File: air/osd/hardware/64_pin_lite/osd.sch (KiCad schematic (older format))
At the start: 0 parts

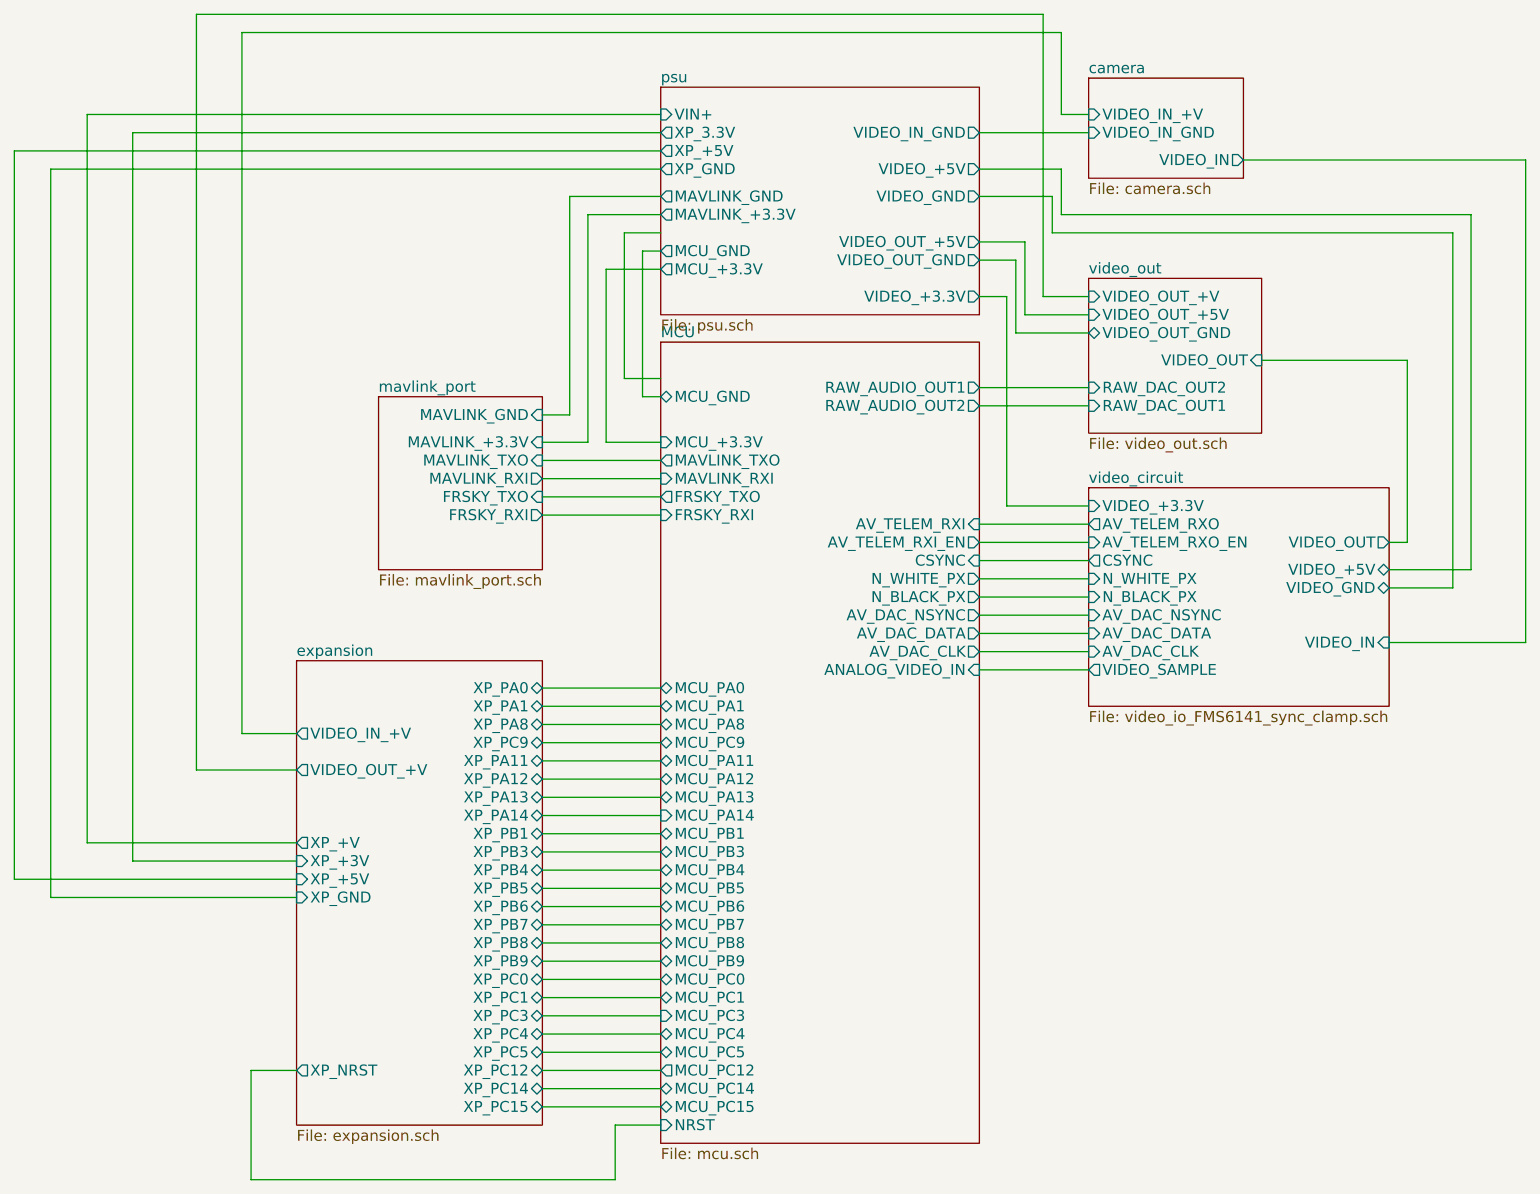
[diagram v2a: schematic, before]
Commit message: added links for isolted port and other mods
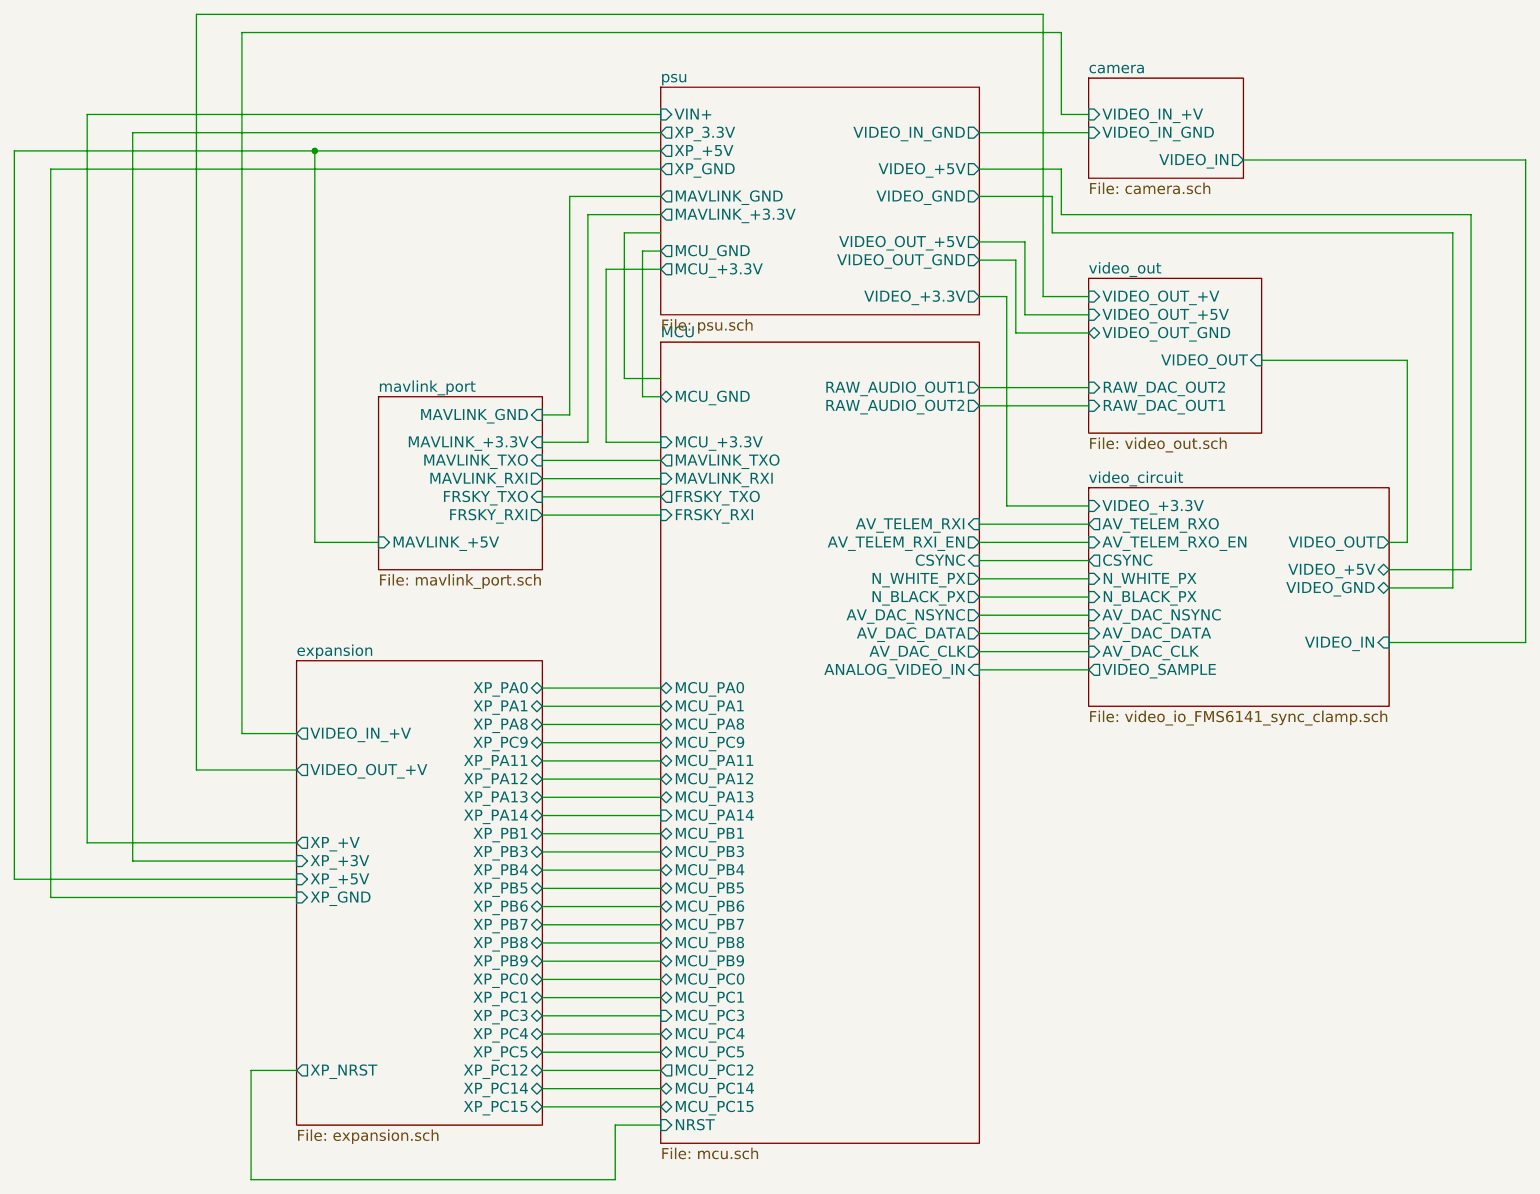
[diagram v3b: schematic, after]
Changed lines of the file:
@@
-EESchema Schematic File Version 2  date Sun 30 Nov 2014 15:34:12 GMT
+EESchema Schematic File Version 2  date Mon 01 Dec 2014 08:28:41 GMT
 LIBS:power
 LIBS:device
@@
 Sheet 1 8
 Title ""
-Date "30 nov 2014"
+Date "1 dec 2014"
 Rev ""
 Comp ""
@@
 Comment4 ""
 $EndDescr
-Wire Wire Line
-	4700 6800 4450 6800
-Wire Wire Line
-	4450 6800 4450 7100
-Wire Wire Line
-	4450 7100 2450 7100
-Wire Wire Line
-	2450 7100 2450 6500
-Wire Wire Line
-	2450 6500 2700 6500
-Wire Wire Line
-	4700 1350 1800 1350
-Wire Wire Line
-	1800 1350 1800 5350
-Wire Wire Line
-	1800 5350 2700 5350
-Wire Wire Line
-	4700 2100 4400 2100
-Wire Wire Line
-	4400 2100 4400 3050
-Wire Wire Line
-	4400 3050 4700 3050
-Wire Wire Line
-	7050 1250 6900 1250
-Wire Wire Line
-	6900 1250 6900 800
-Wire Wire Line
-	6900 800  2400 800
-Wire Wire Line
-	2400 800  2400 4650
-Wire Wire Line
-	2400 4650 2700 4650
-Wire Wire Line
-	4700 1250 1550 1250
-Wire Wire Line
-	1550 1250 1550 5250
-Wire Wire Line
-	1550 5250 2700 5250
+Connection ~ 2800 1450
+Wire Wire Line
+	2800 1450 2800 3600
+Wire Wire Line
+	2800 3600 3150 3600
+Wire Wire Line
+	4700 2700 4500 2700
+Wire Wire Line
+	7050 3400 6600 3400
+Wire Wire Line
+	6600 3400 6600 2250
+Wire Wire Line
+	6600 2250 6450 2250
+Wire Wire Line
+	4700 1800 4300 1800
+Wire Wire Line
+	4300 1800 4300 3050
+Wire Wire Line
+	4300 3050 4050 3050
+Wire Wire Line
+	7050 2250 6800 2250
+Wire Wire Line
+	6800 2250 6800 700
+Wire Wire Line
+	6800 700  2150 700
+Wire Wire Line
+	2150 700  2150 4850
+Wire Wire Line
+	2150 4850 2700 4850
+Wire Wire Line
+	4050 2900 4200 2900
+Wire Wire Line
+	4200 2900 4200 1700
+Wire Wire Line
+	4200 1700 4700 1700
+Wire Wire Line
+	7050 2750 6450 2750
+Wire Wire Line
+	4700 1550 1350 1550
+Wire Wire Line
+	1350 1550 1350 5550
+Wire Wire Line
+	1350 5550 2700 5550
+Wire Wire Line
+	4700 3450 4050 3450
+Wire Wire Line
+	4700 3250 4050 3250
+Wire Wire Line
+	4700 1900 4500 1900
+Wire Wire Line
+	4500 1900 4500 2700
+Wire Wire Line
+	4050 6600 4700 6600
+Wire Wire Line
+	4050 6400 4700 6400
+Wire Wire Line
+	4050 6200 4700 6200
+Wire Wire Line
+	4050 6000 4700 6000
+Wire Wire Line
+	4050 5800 4700 5800
+Wire Wire Line
+	4050 5600 4700 5600
+Wire Wire Line
+	4050 5400 4700 5400
+Wire Wire Line
+	4050 5200 4700 5200
+Wire Wire Line
+	4050 5000 4700 5000
+Wire Wire Line
+	4050 4800 4700 4800
+Wire Wire Line
+	4050 4600 4700 4600
+Wire Wire Line
+	4050 4400 4700 4400
+Wire Wire Line
+	7050 4200 6450 4200
+Wire Wire Line
+	6450 4100 7050 4100
+Wire Wire Line
+	7050 3900 6450 3900
+Wire Wire Line
+	7050 3700 6450 3700
+Wire Wire Line
+	7050 3500 6450 3500
+Wire Wire Line
+	7050 2450 6650 2450
+Wire Wire Line
+	6650 2450 6650 2050
+Wire Wire Line
+	6650 2050 6450 2050
+Wire Wire Line
+	8700 3750 9150 3750
+Wire Wire Line
+	9150 3750 9150 1800
+Wire Wire Line
+	9150 1800 6900 1800
+Wire Wire Line
+	6900 1800 6900 1550
+Wire Wire Line
+	6900 1550 6450 1550
+Wire Wire Line
+	6450 1350 7050 1350
+Wire Wire Line
+	6450 1700 6850 1700
+Wire Wire Line
+	6850 1700 6850 1900
+Wire Wire Line
+	6850 1900 9050 1900
+Wire Wire Line
+	9050 1900 9050 3850
+Wire Wire Line
+	9050 3850 8700 3850
+Wire Wire Line
+	6450 1950 6700 1950
+Wire Wire Line
+	6700 1950 6700 2350
+Wire Wire Line
+	6700 2350 7050 2350
+Wire Wire Line
+	8000 2600 8800 2600
+Wire Wire Line
+	8800 2600 8800 3600
+Wire Wire Line
+	8800 3600 8700 3600
+Wire Wire Line
+	7050 3600 6450 3600
+Wire Wire Line
+	7050 3800 6450 3800
+Wire Wire Line
+	6450 4000 7050 4000
+Wire Wire Line
+	7900 1500 9450 1500
+Wire Wire Line
+	9450 1500 9450 4150
+Wire Wire Line
+	9450 4150 8700 4150
+Wire Wire Line
+	6450 4300 7050 4300
+Wire Wire Line
+	4050 4500 4700 4500
+Wire Wire Line
+	4050 4700 4700 4700
+Wire Wire Line
+	4050 4900 4700 4900
+Wire Wire Line
+	4050 5100 4700 5100
+Wire Wire Line
+	4050 5300 4700 5300
+Wire Wire Line
+	4050 5500 4700 5500
+Wire Wire Line
+	4050 5700 4700 5700
+Wire Wire Line
+	4050 5900 4700 5900
+Wire Wire Line
+	4050 6100 4700 6100
+Wire Wire Line
+	4050 6300 4700 6300
+Wire Wire Line
+	4050 6500 4700 6500
+Wire Wire Line
+	4050 6700 4700 6700
+Wire Wire Line
+	4700 2800 4600 2800
+Wire Wire Line
+	4600 2800 4600 2000
+Wire Wire Line
+	4600 2000 4700 2000
+Wire Wire Line
+	4700 3150 4050 3150
+Wire Wire Line
+	4700 3350 4050 3350
+Wire Wire Line
+	2700 5450 1150 5450
+Wire Wire Line
+	1150 5450 1150 1450
+Wire Wire Line
+	1150 1450 4700 1450
 Wire Wire Line
 	6450 2850 7050 2850
 Wire Wire Line
-	4700 1450 1150 1450
-Wire Wire Line
-	1150 1450 1150 5450
-Wire Wire Line
-	1150 5450 2700 5450
-Wire Wire Line
-	4700 3350 4050 3350
-Wire Wire Line
-	4700 3150 4050 3150
-Wire Wire Line
-	4700 2000 4600 2000
-Wire Wire Line
-	4600 2000 4600 2800
-Wire Wire Line
-	4600 2800 4700 2800
-Wire Wire Line
-	4050 6700 4700 6700
-Wire Wire Line
-	4050 6500 4700 6500
-Wire Wire Line
-	4050 6300 4700 6300
-Wire Wire Line
-	4050 6100 4700 6100
-Wire Wire Line
-	4050 5900 4700 5900
-Wire Wire Line
-	4050 5700 4700 5700
-Wire Wire Line
-	4050 5500 4700 5500
-Wire Wire Line
-	4050 5300 4700 5300
-Wire Wire Line
-	4050 5100 4700 5100
-Wire Wire Line
-	4050 4900 4700 4900
-Wire Wire Line
-	4050 4700 4700 4700
-Wire Wire Line
-	4050 4500 4700 4500
-Wire Wire Line
-	6450 4300 7050 4300
-Wire Wire Line
-	8700 4150 9450 4150
-Wire Wire Line
-	9450 4150 9450 1500
-Wire Wire Line
-	9450 1500 7900 1500
-Wire Wire Line
-	6450 4000 7050 4000
-Wire Wire Line
-	7050 3800 6450 3800
-Wire Wire Line
-	7050 3600 6450 3600
-Wire Wire Line
-	8700 3600 8800 3600
-Wire Wire Line
-	8800 3600 8800 2600
-Wire Wire Line
-	8800 2600 8000 2600
-Wire Wire Line
-	7050 2350 6700 2350
-Wire Wire Line
-	6700 2350 6700 1950
-Wire Wire Line
-	6700 1950 6450 1950
-Wire Wire Line
-	8700 3850 9050 3850
-Wire Wire Line
-	9050 3850 9050 1900
-Wire Wire Line
-	9050 1900 6850 1900
-Wire Wire Line
-	6850 1900 6850 1700
-Wire Wire Line
-	6850 1700 6450 1700
-Wire Wire Line
-	6450 1350 7050 1350
-Wire Wire Line
-	6450 1550 6900 1550
-Wire Wire Line
-	6900 1550 6900 1800
-Wire Wire Line
-	6900 1800 9150 1800
-Wire Wire Line
-	9150 1800 9150 3750
-Wire Wire Line
-	9150 3750 8700 3750
-Wire Wire Line
-	6450 2050 6650 2050
-Wire Wire Line
-	6650 2050 6650 2450
-Wire Wire Line
-	6650 2450 7050 2450
-Wire Wire Line
-	7050 3500 6450 3500
-Wire Wire Line
-	7050 3700 6450 3700
-Wire Wire Line
-	7050 3900 6450 3900
-Wire Wire Line
-	6450 4100 7050 4100
-Wire Wire Line
-	7050 4200 6450 4200
-Wire Wire Line
-	4050 4400 4700 4400
-Wire Wire Line
-	4050 4600 4700 4600
-Wire Wire Line
-	4050 4800 4700 4800
-Wire Wire Line
-	4050 5000 4700 5000
-Wire Wire Line
-	4050 5200 4700 5200
-Wire Wire Line
-	4050 5400 4700 5400
-Wire Wire Line
-	4050 5600 4700 5600
-Wire Wire Line
-	4050 5800 4700 5800
-Wire Wire Line
-	4050 6000 4700 6000
-Wire Wire Line
-	4050 6200 4700 6200
-Wire Wire Line
-	4050 6400 4700 6400
-Wire Wire Line
-	4050 6600 4700 6600
-Wire Wire Line
-	4500 1900 4500 2700
-Wire Wire Line
-	4500 1900 4700 1900
-Wire Wire Line
-	4700 3250 4050 3250
-Wire Wire Line
-	4700 3450 4050 3450
-Wire Wire Line
-	2700 5550 1350 5550
-Wire Wire Line
-	1350 5550 1350 1550
-Wire Wire Line
-	1350 1550 4700 1550
-Wire Wire Line
-	7050 2750 6450 2750
-Wire Wire Line
-	4700 1700 4200 1700
-Wire Wire Line
-	4200 1700 4200 2900
-Wire Wire Line
-	4200 2900 4050 2900
-Wire Wire Line
-	2700 4850 2150 4850
-Wire Wire Line
-	2150 4850 2150 700
-Wire Wire Line
-	2150 700  6800 700
-Wire Wire Line
-	6800 700  6800 2250
-Wire Wire Line
-	6800 2250 7050 2250
-Wire Wire Line
-	4050 3050 4300 3050
-Wire Wire Line
-	4300 3050 4300 1800
-Wire Wire Line
-	4300 1800 4700 1800
-Wire Wire Line
-	6450 2250 6600 2250
-Wire Wire Line
-	6600 2250 6600 3400
-Wire Wire Line
-	6600 3400 7050 3400
-Wire Wire Line
-	4500 2700 4700 2700
+	2700 5250 1550 5250
+Wire Wire Line
+	1550 5250 1550 1250
+Wire Wire Line
+	1550 1250 4700 1250
+Wire Wire Line
+	2700 4650 2400 4650
+Wire Wire Line
+	2400 4650 2400 800
+Wire Wire Line
+	2400 800  6900 800
+Wire Wire Line
+	6900 800  6900 1250
+Wire Wire Line
+	6900 1250 7050 1250
+Wire Wire Line
+	4700 3050 4400 3050
+Wire Wire Line
+	4400 3050 4400 2100
+Wire Wire Line
+	4400 2100 4700 2100
+Wire Wire Line
+	2700 5350 1800 5350
+Wire Wire Line
+	1800 5350 1800 1350
+Wire Wire Line
+	1800 1350 4700 1350
+Wire Wire Line
+	2700 6500 2450 6500
+Wire Wire Line
+	2450 6500 2450 7100
+Wire Wire Line
+	2450 7100 4450 7100
+Wire Wire Line
+	4450 7100 4450 6800
+Wire Wire Line
+	4450 6800 4700 6800
 $Sheet
 S 4700 2500 1750 4400
@@
 F6 "FRSKY_RXI" O R 4050 3450 60
 F7 "MAVLINK_+3.3V" I R 4050 3050 60
-$EndSheet
-$Sheet
+F8 "MAVLINK_+5V" I L 3150 3600 60
+$EndSheet
+$Sheet
